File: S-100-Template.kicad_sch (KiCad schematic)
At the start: 3 parts

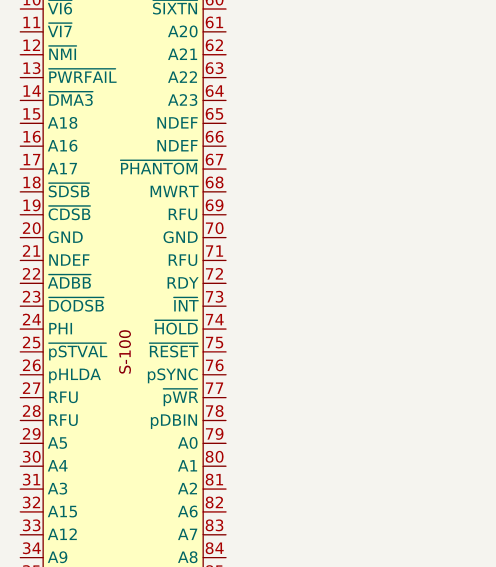
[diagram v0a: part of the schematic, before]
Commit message: Correct spelling of ADSB
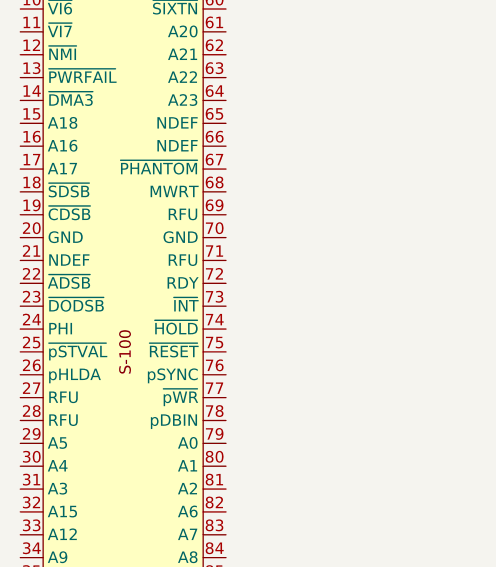
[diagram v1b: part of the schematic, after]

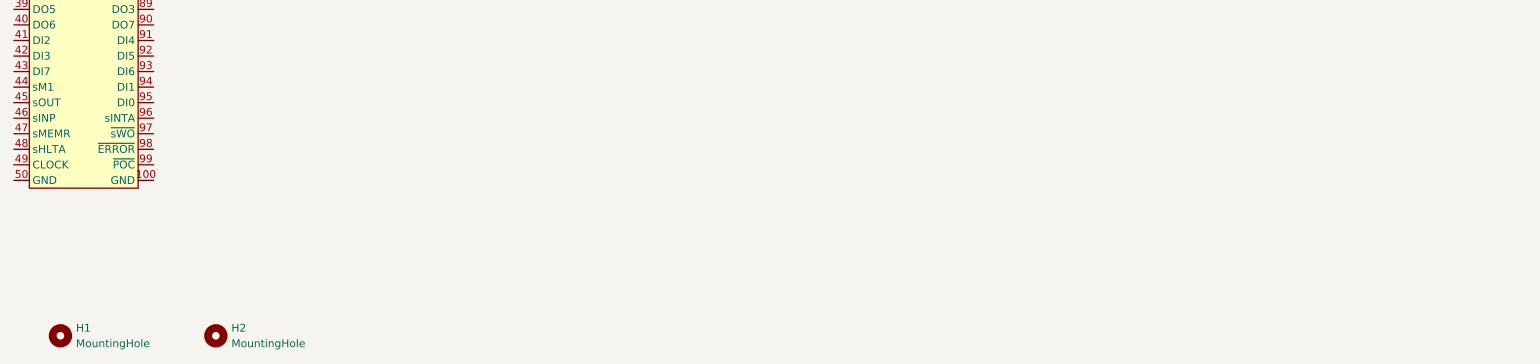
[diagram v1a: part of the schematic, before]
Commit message: Cleanup paste layer Add card ejector info
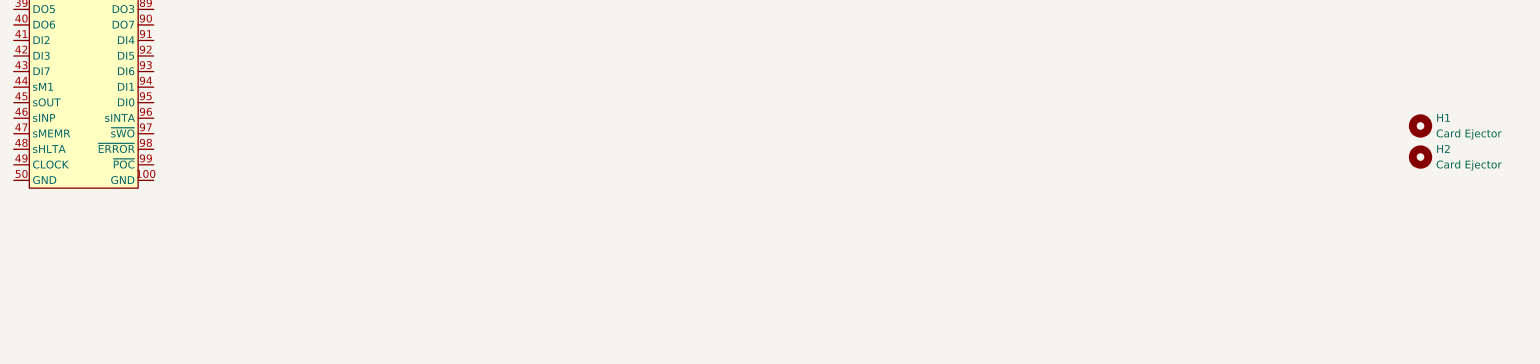
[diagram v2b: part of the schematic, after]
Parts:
- H1, H2: value MountingHole -> Card Ejector; Digi-Key_PN (none) -> 492-1025-ND; Manufacturer   (none) -> Bivar Inc.; now in the parts list
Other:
- moved on the sheet: H1, H2
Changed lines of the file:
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@@
 	(symbol
 		(lib_id "Mechanical:MountingHole")
-		(at 69.85 187.96 0)
+		(at 266.7 158.75 0)
 		(unit 1)
 		(exclude_from_sim no)
-		(in_bom no)
+		(in_bom yes)
 		(on_board yes)
 		(dnp no)
 		(fields_autoplaced yes)
 		(property "Reference" "H2"
-			(at 72.39 186.6899 0)
+			(at 269.24 157.4799 0)
 			(effects
 				(font
@@
 			)
 		)
-		(property "Value" "MountingHole"
-			(at 72.39 189.2299 0)
+		(property "Value" "Card Ejector"
+			(at 269.24 160.0199 0)
 			(effects
 				(font
@@
 		)
 		(property "Footprint" "MountingHole:MountingHole_2.5mm"
-			(at 69.85 187.96 0)
+			(at 266.7 158.75 0)
 			(effects
 				(font
@@
 			)
 		)
-		(property "Datasheet" "~"
-			(at 69.85 187.96 0)
+		(property "Datasheet" "https://mm.digikey.com/Volume0/opasdata/d220001/medias/docus/6722/CP-2X_D1.pdf"
+			(at 266.7 158.75 0)
 			(effects
 				(font
@@
 		)
 		(property "Description" "Mounting Hole without connection"
-			(at 69.85 187.96 0)
+			(at 266.7 158.75 0)
+			(effects
+				(font
+					(size 1.27 1.27)
+				)
+				(hide yes)
+			)
+		)
+		(property "Digi-Key_PN" "492-1025-ND"
+			(at 266.7 158.75 0)
+			(effects
+				(font
+					(size 1.27 1.27)
+				)
+				(hide yes)
+			)
+		)
+		(property "Manufacturer  " "Bivar Inc."
+			(at 266.7 158.75 0)
 			(effects
 				(font
@@
 	)
 	(symbol
+		(lib_name "MountingHole_1")
 		(lib_id "Mechanical:MountingHole")
-		(at 44.45 187.96 0)
+		(at 266.7 153.67 0)
 		(unit 1)
 		(exclude_from_sim no)
-		(in_bom no)
+		(in_bom yes)
 		(on_board yes)
 		(dnp no)
 		(fields_autoplaced yes)
 		(property "Reference" "H1"
-			(at 46.99 186.6899 0)
+			(at 269.24 152.3999 0)
 			(effects
 				(font
@@
 			)
 		)
-		(property "Value" "MountingHole"
-			(at 46.99 189.2299 0)
+		(property "Value" "Card Ejector"
+			(at 269.24 154.9399 0)
 			(effects
 				(font
@@
 		)
 		(property "Footprint" "MountingHole:MountingHole_2.5mm"
-			(at 44.45 187.96 0)
+			(at 266.7 153.67 0)
 			(effects
 				(font
@@
 			)
 		)
-		(property "Datasheet" "~"
-			(at 44.45 187.96 0)
+		(property "Datasheet" "https://mm.digikey.com/Volume0/opasdata/d220001/medias/docus/6722/CP-2X_D1.pdf"
+			(at 266.7 153.67 0)
 			(effects
 				(font
@@
 		)
 		(property "Description" "Mounting Hole without connection"
-			(at 44.45 187.96 0)
+			(at 266.7 153.67 0)
 			(effects
 				(font
+					(size 1.27 1.27)
+				)
+				(hide yes)
+			)
+		)
+		(property "Digi-Key_PN" "492-1025-ND"
+			(at 266.7 153.67 0)
+			(effects
+				(font
+					(size 1.27 1.27)
+				)
+				(hide yes)
+			)
+		)
+		(property "Manufacturer  " "Bivar Inc."
+			(at 266.7 153.67 0)
+			(effects
+				(font

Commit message: DRC cleanup
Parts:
- H1, H2: Manufacturer (none) -> Bivar Inc.; Manufacturer   Bivar Inc. -> (none)
- J1: value ~ -> (none)
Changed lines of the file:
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@@
 			)
 		)
-		(property "Value" "~"
+		(property "Value" ""
 			(at 48.26 34.29 0)
 			(effects
@@
 			)
 		)
-		(property "Manufacturer  " "Bivar Inc."
+		(property "Manufacturer" "Bivar Inc."
 			(at 266.7 158.75 0)
 			(effects
@@
 			)
 		)
-		(property "Manufacturer  " "Bivar Inc."
-			(at 266.7 153.67 0)
-			(effects
+		(property "Manufacturer" "Bivar Inc."
+			(at 266.7 153.67 0)
+			(effects

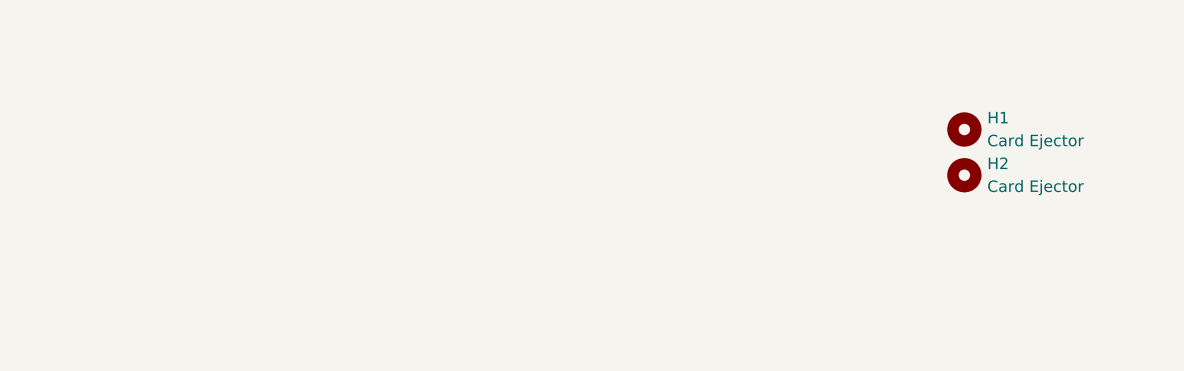
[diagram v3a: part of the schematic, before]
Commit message: Change size to to 5x10
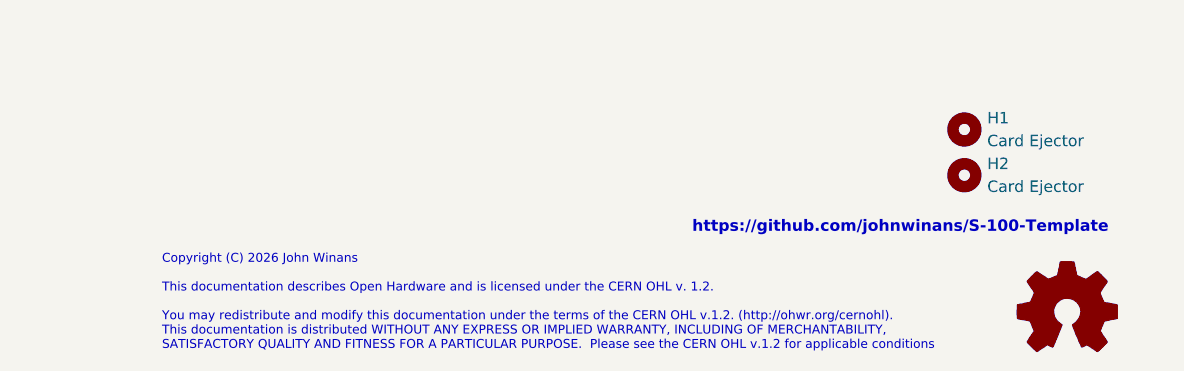
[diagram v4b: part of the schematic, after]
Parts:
- added LOGO1: OSHW_Logo, Symbol:OSHW-Logo_11.4x12mm_SilkScreen, symbol Graphic:Logo_Open_Hardware_Small
- J1: value (none) -> ~
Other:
- note added: "Copyright (C) 2026 John Winans This documentation describes Open Hardware and is licensed under the CERN OHL v. 1.2. You may redistribute and modify this documentation under the terms of the CERN OHL v.1.2. (http://ohwr.org/cernohl). This documentation is distributed WITHOUT ANY EXPRESS OR IMPLIED WARRANTY, INCLUDING OF MERCHANTABILITY, SATISFACTORY QUALITY AND FITNESS FOR A PARTICULAR PURPOSE. P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"
- note added: "https://github.com/johnwinans/S-100-Template"
- title: (none) -> S-100 Card Template
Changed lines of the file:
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@@
 	(generator_version "9.0")
 	(paper "A4")
+	(title_block
+		(title "S-100 Card Template")
+		(date "2026-04-08")
+		(rev "1.1")
+	)
+	(text "Copyright (C) 2026 John Winans\n\nThis documentation describes Open Hardware and is licensed under the CERN OHL v. 1.2.\n\nYou may redistribute and modify this documentation under the terms of the CERN OHL v.1.2. (http://ohwr.org/cernohl). \nThis documentation is distributed WITHOUT ANY EXPRESS OR IMPLIED WARRANTY, INCLUDING OF MERCHANTABILITY, \nSATISFACTORY QUALITY AND FITNESS FOR A PARTICULAR PURPOSE.  Please see the CERN OHL v.1.2 for applicable conditions"
+		(exclude_from_sim no)
+		(at 177.546 178.308 0)
+		(effects
+			(font
+				(size 0.9906 0.9906)
+			)
+			(justify left bottom)
+		)
+	)
+	(text "https://github.com/johnwinans/S-100-Template"
+		(exclude_from_sim no)
+		(at 259.588 164.592 0)
+		(effects
+			(font
+				(size 1.27 1.27)
+				(thickness 0.254)
+				(bold yes)
+			)
+		)
+	)
+	(symbol
+		(lib_id "Graphic:Logo_Open_Hardware_Small")
+		(at 278.13 173.99 0)
+		(unit 1)
+		(exclude_from_sim no)
+		(in_bom no)
+		(on_board yes)
+		(dnp no)
+		(property "Reference" "LOGO1"
+			(at 278.13 167.005 0)
+			(effects
+				(font
+					(size 1.27 1.27)
+				)
+				(hide yes)
+			)
+		)
+		(property "Value" "OSHW_Logo"
+			(at 278.13 179.705 0)
+			(effects
+				(font
+					(size 1.27 1.27)
+				)
+				(hide yes)
+			)
+		)
+		(property "Footprint" "Symbol:OSHW-Logo_11.4x12mm_SilkScreen"
+			(at 278.13 173.99 0)
+			(effects
+				(font
+					(size 1.27 1.27)
+				)
+				(hide yes)
+			)
+		)
+		(property "Datasheet" ""
+			(at 278.13 173.99 0)
+			(effects
+				(font
+					(size 1.27 1.27)
+				)
+				(hide yes)
+			)
+		)
+		(property "Description" ""
+			(at 278.13 173.99 0)
+			(effects
+				(font
+					(size 1.27 1.27)
+				)
+			)
+		)
+		(instances
+			(project "S-100-Template"
+				(path "/e6802e0a-d78e-48fb-9644-7dc83bb4bf35"
+					(reference "LOGO1")
+					(unit 1)
+				)
+			)
+		)
+	)
 	(symbol
 		(lib_id "S100:S100-Edge-Connector")
@@
 			)
 		)
-		(property "Value" ""
+		(property "Value" "~"
 			(at 48.26 34.29 0)
 			(effects
@@
 		)
 		(property "Description" ""
+			(at 48.26 99.06 0)
+			(effects
+				(font
+					(size 1.27 1.27)
+				)
+				(hide yes)
+			)
+		)
+		(property "Manufacturer  " ""
 			(at 48.26 99.06 0)
 			(effects
@@
 			)
 		)
-		(property "Description" "Mounting Hole without connection"
+		(property "Description" "Card Ejector"
 			(at 266.7 158.75 0)
 			(effects
@@
 		)
 		(property "Manufacturer" "Bivar Inc."
+			(at 266.7 158.75 0)
+			(effects
+				(font
+					(size 1.27 1.27)
+				)
+				(hide yes)
+			)
+		)
+		(property "Manufacturer  " ""
 			(at 266.7 158.75 0)
 			(effects
@@
 			)
 		)
-		(property "Description" "Mounting Hole without connection"
+		(property "Description" "Card Ejector"
 			(at 266.7 153.67 0)
 			(effects
@@
 			(at 266.7 153.67 0)
 			(effects
+				(font
+					(size 1.27 1.27)
+				)
+				(hide yes)
+			)
+		)
+		(property "Manufacturer  " ""
+			(at 266.7 153.67 0)
+			(effects
